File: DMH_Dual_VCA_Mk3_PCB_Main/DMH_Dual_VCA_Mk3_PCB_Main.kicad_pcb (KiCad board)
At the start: 2 copper layers, 49 x 175 mm, 95 parts, among them J1 TRS_Jack_6.35mm_Sw, J100 IDC_02x05, J11 Conn_01x06, J12 Conn_01x08, J13 Conn_01x06, J18 Conn_02x03_Odd_Even, J19 Conn_02x03_Odd_Even, J2 TRS_Jack_6.35mm_Sw, J20 Conn_01x01, J200 IDC_02x05, J21 Conn_01x08, J22 Conn_02x03_Odd_Even, J23 Conn_02x03_Odd_Even, J3 TRS_Jack_6.35mm_Sw, J4 TRS_Jack_6.35mm_Sw, J5 TRS_Jack_6.35mm_Sw, J6 TRS_Jack_6.35mm_Sw, J7 TRS_Jack_6.35mm_Sw, J8 TRS_Jack_6.35mm_Sw, J9 TRS_Jack_6.35mm_Sw, Q10 BC548, Q11 BC548, Q12 BC548, Q9 BC548, U1 LM4040LP-5, U10 TL074, U2 LM4040LP-5, U3 TL074, U4 TL072

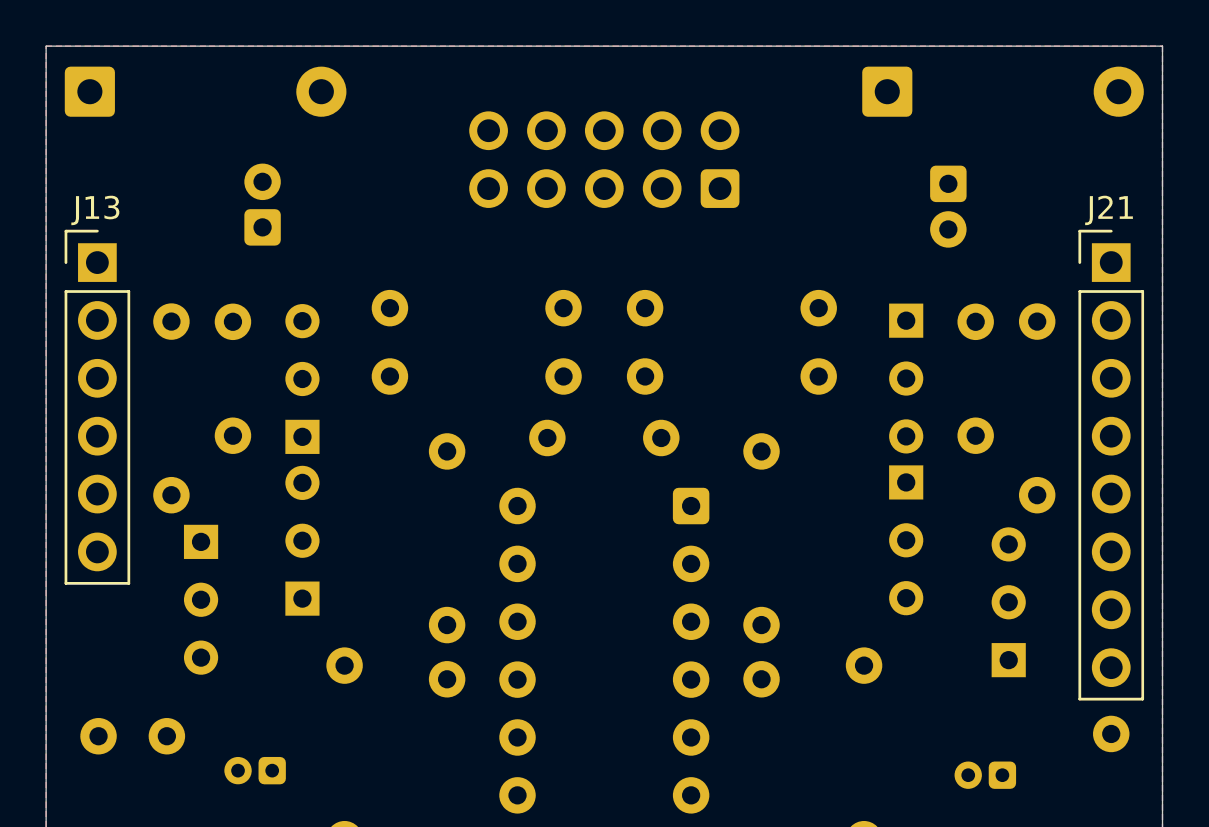
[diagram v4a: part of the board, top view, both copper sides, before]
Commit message: Started Main PCB routing
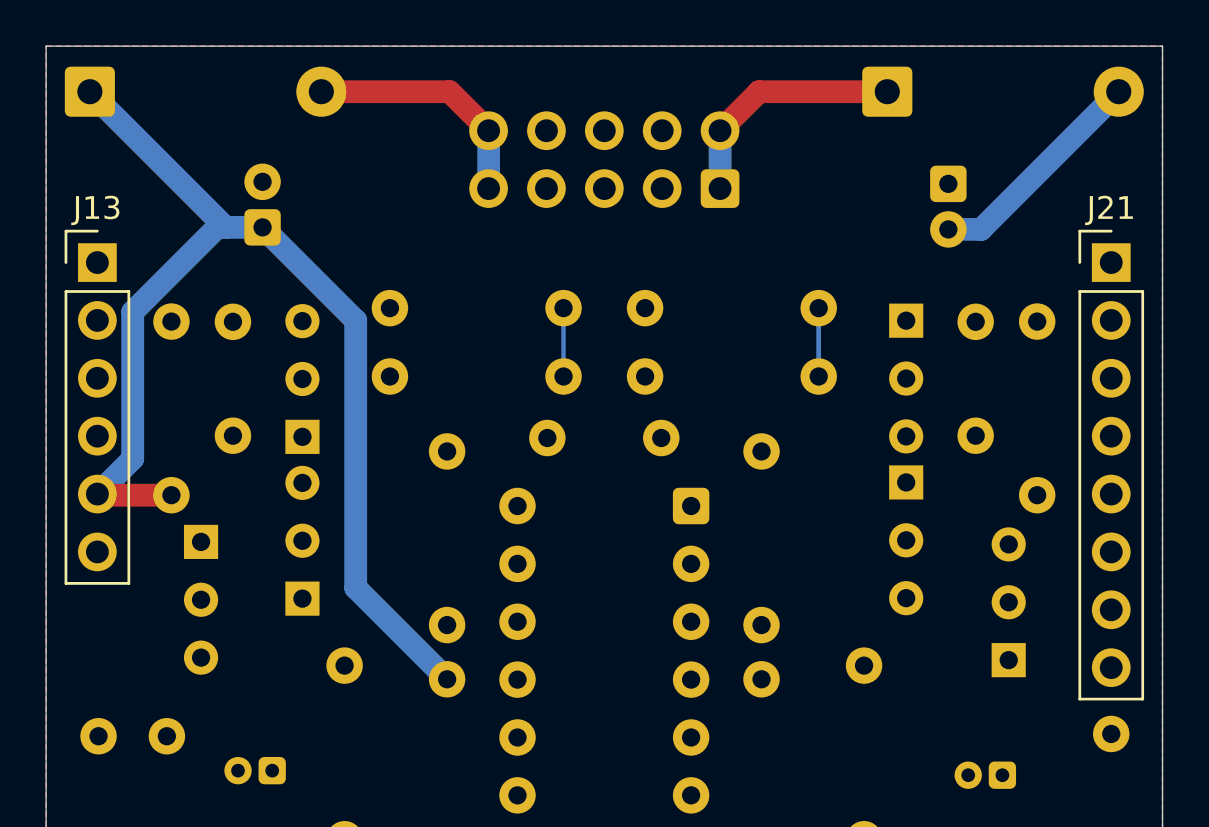
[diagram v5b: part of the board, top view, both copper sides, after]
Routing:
- net +12V: track 0.00 -> 50.8 mm
- net Net-(D4-A): track 0.00 -> 10.6 mm
- net Net-(D3-K): track 0.00 -> 10.6 mm
- net -12V: track 0.00 -> 9.98 mm
- net /Clipping/Clip_Sw_p5_m: track 0.00 -> 3.00 mm
- net /Clipping/Clip_Sw_p2_m: track 0.00 -> 3.00 mm
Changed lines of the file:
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@@
 		)
+	)
+	(segment
+		(start 97.58 44.5)
+		(end 91.535112 50.544888)
+		(width 1)
+		(layer "B.Cu")
+		(net "-12V")
+	)
+	(segment
+		(start 91.535112 50.544888)
+		(end 90.1 50.544888)
+		(width 1)
+		(layer "B.Cu")
+		(net "-12V")
+	)
+	(segment
+		(start 56 62.21)
+		(end 52.8 62.21)
+		(width 1)
+		(layer "F.Cu")
+		(net "+12V")
+	)
+	(segment
+		(start 52.8 62.21)
+		(end 52.75 62.16)
+		(width 1)
+		(layer "F.Cu")
+		(net "+12V")
+	)
+	(segment
+		(start 64.09 66.28)
+		(end 68.1 70.29)
+		(width 1)
+		(layer "B.Cu")
+		(net "+12V")
+	)
+	(segment
+		(start 64.09 54.545113)
+		(end 64.09 66.28)
+		(width 1)
+		(layer "B.Cu")
+		(net "+12V")
+	)
+	(segment
+		(start 52.42 44.5)
+		(end 58.375113 50.455113)
+		(width 1)
+		(layer "B.Cu")
+		(net "+12V")
+	)
+	(segment
+		(start 60 50.455113)
+		(end 64.09 54.545113)
+		(width 1)
+		(layer "B.Cu")
+		(net "+12V")
+	)
+	(segment
+		(start 54.3 54.168679)
+		(end 58.013566 50.455113)
+		(width 1)
+		(layer "B.Cu")
+		(net "+12V")
+	)
+	(segment
+		(start 54.3 60.61)
+		(end 54.3 54.168679)
+		(width 1)
+		(layer "B.Cu")
+		(net "+12V")
+	)
+	(segment
+		(start 58.375113 50.455113)
+		(end 60 50.455113)
+		(width 1)
+		(layer "B.Cu")
+		(net "+12V")
+	)
+	(segment
+		(start 58.013566 50.455113)
+		(end 58.375113 50.455113)
+		(width 1)
+		(layer "B.Cu")
+		(net "+12V")
+	)
+	(segment
+		(start 52.75 62.16)
+		(end 54.3 60.61)
+		(width 1)
+		(layer "B.Cu")
+		(net "+12V")
+	)
+	(segment
+		(start 84.41 57)
+		(end 84.41 54)
+		(width 0.2)
+		(layer "B.Cu")
+		(net "/Clipping/Clip_Sw_p2_m")
+	)
+	(segment
+		(start 73.21 57)
+		(end 73.21 54)
+		(width 0.2)
+		(layer "B.Cu")
+		(net "/Clipping/Clip_Sw_p5_m")
+	)
+	(segment
+		(start 87.42 44.5)
+		(end 81.7925 44.5)
+		(width 1)
+		(layer "F.Cu")
+		(net "Net-(D3-K)")
+	)
+	(segment
+		(start 81.7925 44.5)
+		(end 80.08 46.2125)
+		(width 1)
+		(layer "F.Cu")
+		(net "Net-(D3-K)")
+	)
+	(segment
+		(start 80.08 48.7525)
+		(end 80.08 46.2125)
+		(width 1)
+		(layer "B.Cu")
+		(net "Net-(D3-K)")
+	)
+	(segment
+		(start 62.58 44.5)
+		(end 68.2075 44.5)
+		(width 1)
+		(layer "F.Cu")
+		(net "Net-(D4-A)")
+	)
+	(segment
+		(start 68.2075 44.5)
+		(end 69.92 46.2125)
+		(width 1)
+		(layer "F.Cu")
+		(net "Net-(D4-A)")
+	)
+	(segment
+		(start 69.92 48.7525)
+		(end 69.92 46.2125)
+		(width 1)
+		(layer "B.Cu")
+		(net "Net-(D4-A)")
 	)
 	(zone

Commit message: Added jumpers to normalize CV inputs B to A
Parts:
- added JP2: Jumper, Connector_PinHeader_2.54mm:PinHeader_1x03_P2.54mm_Vertical, B.Cu at (57.3, 160.6)
- added JP3: Jumper, Connector_PinHeader_2.54mm:PinHeader_1x03_P2.54mm_Vertical, B.Cu at (61.0, 160.6)
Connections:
- J200 pad 3: /CV_In_B2_N_m -> Net-(J200-Pin_3)
- J200 pad 7: /CV_In_B1_N_m -> Net-(J200-Pin_7)
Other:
- board text added: "+5V"
- board text added: "CV Ax T"
- board text added: "CV Bx TN"
- board text added: "CV PT TN"
- board text added: "J200"
- board text added: "Jumper:"
- board text added: "Jumpers:"

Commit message: Fixed -5V supply circuit mistake
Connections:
- R1 pad 2: +12V -> -12V
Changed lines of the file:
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@@
 			(layers "*.Cu" "*.Mask")
 			(remove_unused_layers no)
-			(net "+12V")
+			(net "-12V")
 			(pintype "passive")
 		)

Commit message: Added jumper to normalize Input B to A
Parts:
- added JP4: Jumper, Connector_PinHeader_2.54mm:PinHeader_1x03_P2.54mm_Vertical, B.Cu at (58.1, 160.6)
- moved J200 4.50 mm to (74.4, 157.3)
- moved JP1 4.50 mm to (93.5, 160.6)
- moved JP2 4.50 mm to (61.8, 160.6)
- moved JP3 4.50 mm to (65.5, 160.6)
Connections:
- J200 pad 2: /Input_B_N_m -> Net-(J200-Pin_2)
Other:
- board text added: "In A T"
- board text added: "In B TN"
- board text added: "JP1:"
- board text added: "JP2/3:"
- board text added: "JP4:"
- board text removed: "Jumper:"
- board text removed: "Jumpers:"
